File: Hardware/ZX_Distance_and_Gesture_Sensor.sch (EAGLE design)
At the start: 48 parts, among them Q1 MMBT2222A, Q2 MOSFET-NCHANNEL2N7002PW, U1 BRM-2508VERT

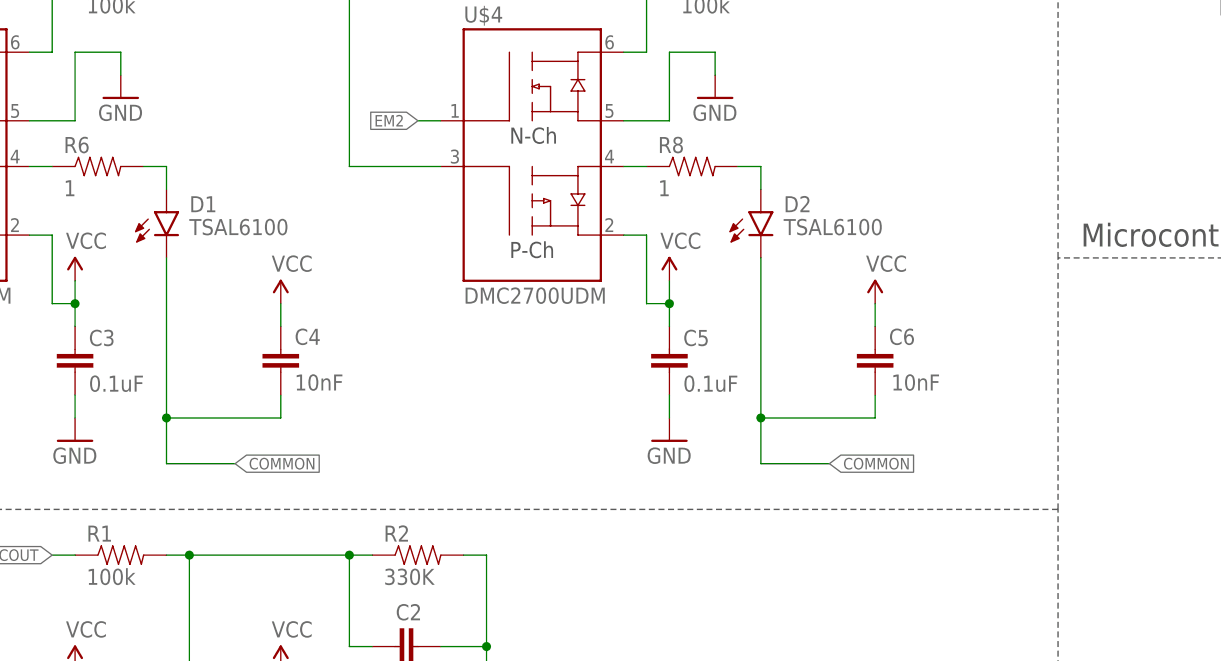
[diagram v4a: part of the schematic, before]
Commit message: Added second option for SMT IR LEDs. Added solder pads for blinders.
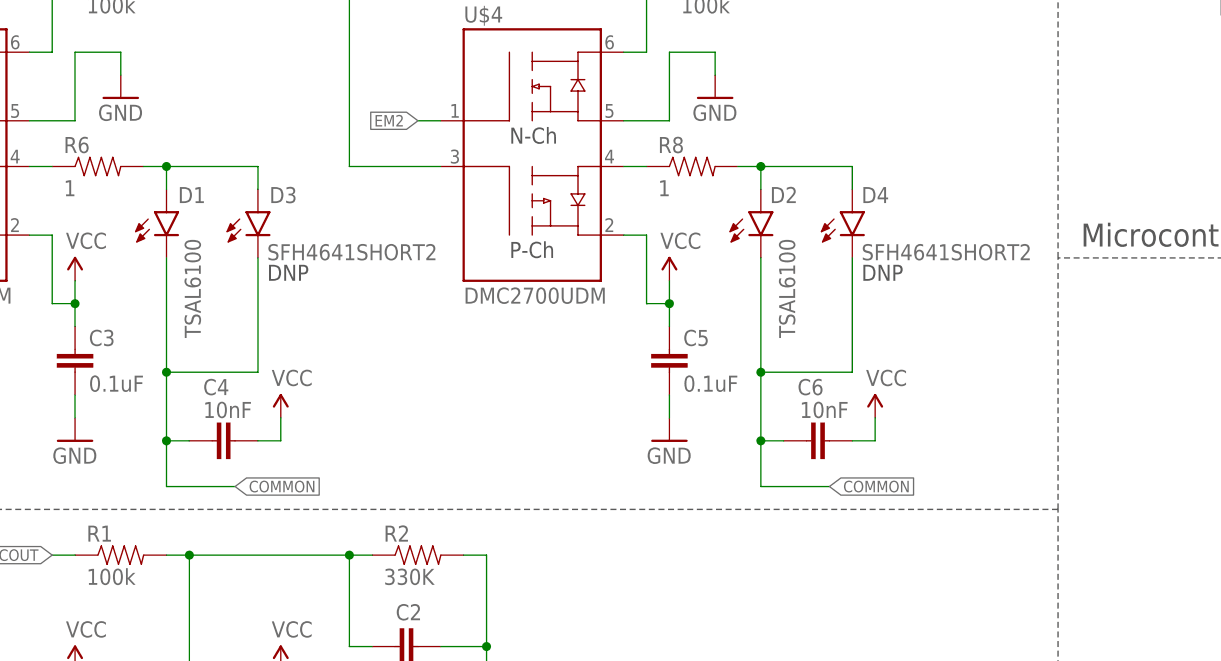
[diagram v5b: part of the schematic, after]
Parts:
- added D3, D4: SFH4641SHORT2, SparkFun-LED:SFH4641SHORT2
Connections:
- net COMMON: now also D3.C, D4.C
- net N$12: now also D4.A
- net N$7: now also D3.A
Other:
- note added: "DNP"
- moved on the sheet: C4, C6
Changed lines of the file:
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@@
 <setting verticaltext="up"/>
 </settings>
-<grid distance="0.1" unitdist="inch" unit="inch" style="lines" multiple="1" display="no" altdistance="0.01" altunitdist="inch" altunit="inch"/>
+<grid distance="0.1" unitdist="inch" unit="inch" style="lines" multiple="1" display="yes" altdistance="0.01" altunitdist="inch" altunit="inch"/>
 <layers>
 <layer number="1" name="Top" color="4" fill="1" visible="no" active="no"/>
@@
 <layer number="111" name="LPC17xx" color="7" fill="1" visible="yes" active="yes"/>
 <layer number="112" name="tSilk" color="7" fill="1" visible="yes" active="yes"/>
+<layer number="113" name="IDFDebug" color="7" fill="1" visible="yes" active="yes"/>
 <layer number="116" name="Patch_BOT" color="9" fill="4" visible="yes" active="yes"/>
 <layer number="121" name="_tsilk" color="7" fill="1" visible="yes" active="yes"/>
@@
 <part name="GND16" library="SparkFun-Aesthetics" deviceset="GND" device=""/>
 <part name="U$6" library="SparkFun-Aesthetics" deviceset="GESTURESENSE_LOGOS" device="TEXT"/>
+<part name="D3" library="SparkFun-LED" deviceset="SFH4641" device="SHORT2"/>
+<part name="D4" library="SparkFun-LED" deviceset="SFH4641" device="SHORT2"/>
 </parts>
 <sheets>
@@
 <text x="50.8" y="149.86" size="1.778" layer="97" align="center-right">DR</text>
 <text x="7.62" y="149.86" size="1.778" layer="97" align="center-right">NC</text>
+<text x="59.436" y="96.52" size="1.778" layer="97">DNP</text>
+<text x="125.476" y="96.52" size="1.778" layer="97">DNP</text>
 </plain>
 <instances>
@@
 <instance part="GND6" gate="1" x="91.44" y="5.08"/>
 <instance part="D1" gate="G$1" x="48.26" y="104.14" smashed="yes">
-<attribute name="NAME" x="50.8" y="104.14" size="1.778" layer="95"/>
-<attribute name="VARIANT" x="50.8" y="101.6" size="1.778" layer="96"/>
+<attribute name="NAME" x="49.53" y="105.156" size="1.778" layer="95"/>
+<attribute name="VARIANT" x="52.07" y="90.17" size="1.778" layer="96" rot="R90"/>
 </instance>
 <instance part="R5" gate="G$1" x="43.18" y="129.54"/>
@@
 <attribute name="VALUE" x="39.624" y="84.201" size="1.778" layer="96"/>
 </instance>
-<instance part="C4" gate="G$1" x="60.96" y="88.9" smashed="yes" rot="R180">
-<attribute name="NAME" x="62.484" y="89.408" size="1.778" layer="95"/>
-<attribute name="VALUE" x="62.484" y="84.328" size="1.778" layer="96"/>
+<instance part="C4" gate="G$1" x="55.88" y="78.74" smashed="yes" rot="R90">
+<attribute name="NAME" x="52.324" y="83.82" size="1.778" layer="95"/>
+<attribute name="VALUE" x="52.324" y="81.28" size="1.778" layer="96"/>
 </instance>
 <instance part="SUPPLY5" gate="G$1" x="38.1" y="96.52"/>
-<instance part="SUPPLY6" gate="G$1" x="60.96" y="93.98"/>
+<instance part="SUPPLY6" gate="G$1" x="60.96" y="81.28"/>
 <instance part="GND7" gate="1" x="38.1" y="78.74"/>
 <instance part="GND8" gate="1" x="43.18" y="116.84"/>
@@
 <attribute name="VALUE" x="105.664" y="84.201" size="1.778" layer="96"/>
 </instance>
-<instance part="C6" gate="G$1" x="127" y="88.9" smashed="yes" rot="R180">
-<attribute name="NAME" x="128.524" y="89.408" size="1.778" layer="95"/>
-<attribute name="VALUE" x="128.778" y="84.328" size="1.778" layer="96"/>
-</instance>
-<instance part="SUPPLY9" gate="G$1" x="127" y="93.98"/>
+<instance part="C6" gate="G$1" x="121.92" y="78.74" smashed="yes" rot="R90">
+<attribute name="NAME" x="118.364" y="83.82" size="1.778" layer="95"/>
+<attribute name="VALUE" x="118.618" y="81.28" size="1.778" layer="96"/>
+</instance>
+<instance part="SUPPLY9" gate="G$1" x="127" y="81.28"/>
 <instance part="SUPPLY10" gate="G$1" x="104.14" y="96.52"/>
 <instance part="GND10" gate="1" x="104.14" y="78.74"/>
@@
 <instance part="SUPPLY11" gate="G$1" x="170.18" y="68.58"/>
 <instance part="D2" gate="G$1" x="114.3" y="104.14" smashed="yes">
-<attribute name="NAME" x="116.84" y="104.14" size="1.778" layer="95"/>
-<attribute name="VARIANT" x="116.84" y="101.6" size="1.778" layer="96"/>
+<attribute name="NAME" x="115.316" y="105.156" size="1.778" layer="95"/>
+<attribute name="VARIANT" x="118.11" y="90.17" size="1.778" layer="96" rot="R90"/>
 </instance>
 <instance part="SUPPLY12" gate="G$1" x="223.52" y="91.44"/>
@@
 <instance part="GND16" gate="1" x="172.72" y="78.74"/>
 <instance part="U$6" gate="G$1" x="127" y="22.86"/>
+<instance part="D3" gate="G$1" x="58.42" y="104.14" smashed="yes">
+<attribute name="NAME" x="59.69" y="105.156" size="1.778" layer="95"/>
+<attribute name="VALUE" x="59.436" y="98.806" size="1.778" layer="96"/>
+</instance>
+<instance part="D4" gate="G$1" x="124.46" y="104.14" smashed="yes">
+<attribute name="NAME" x="125.476" y="105.156" size="1.778" layer="95"/>
+<attribute name="VALUE" x="125.476" y="98.806" size="1.778" layer="96"/>
+</instance>
 </instances>
 <busses>
@@
 <pinref part="U$2" gate="G$1" pin="V+"/>
 <wire x1="60.96" y1="53.34" x2="60.96" y2="50.8" width="0.1524" layer="91"/>
-</segment>
-<segment>
-<pinref part="SUPPLY6" gate="G$1" pin="VCC"/>
-<pinref part="C4" gate="G$1" pin="2"/>
-<wire x1="60.96" y1="93.98" x2="60.96" y2="91.44" width="0.1524" layer="91"/>
 </segment>
 <segment>
@@
 </segment>
 <segment>
-<pinref part="C6" gate="G$1" pin="2"/>
-<pinref part="SUPPLY9" gate="G$1" pin="VCC"/>
-<wire x1="127" y1="91.44" x2="127" y2="93.98" width="0.1524" layer="91"/>
-</segment>
-<segment>
 <pinref part="SUPPLY10" gate="G$1" pin="VCC"/>
 <pinref part="C5" gate="G$1" pin="1"/>
@@
 <wire x1="172.72" y1="86.36" x2="172.72" y2="88.9" width="0.1524" layer="91"/>
 <pinref part="SUPPLY16" gate="G$1" pin="VCC"/>
+</segment>
+<segment>
+<pinref part="C4" gate="G$1" pin="2"/>
+<pinref part="SUPPLY6" gate="G$1" pin="VCC"/>
+<wire x1="58.42" y1="78.74" x2="60.96" y2="78.74" width="0.1524" layer="91"/>
+<wire x1="60.96" y1="78.74" x2="60.96" y2="81.28" width="0.1524" layer="91"/>
+</segment>
+<segment>
+<pinref part="C6" gate="G$1" pin="2"/>
+<pinref part="SUPPLY9" gate="G$1" pin="VCC"/>
+<wire x1="124.46" y1="78.74" x2="127" y2="78.74" width="0.1524" layer="91"/>
+<wire x1="127" y1="78.74" x2="127" y2="81.28" width="0.1524" layer="91"/>
 </segment>
 </net>
@@
 <segment>
 <pinref part="D1" gate="G$1" pin="C"/>
-<wire x1="48.26" y1="99.06" x2="48.26" y2="81.28" width="0.1524" layer="91"/>
-<wire x1="48.26" y1="81.28" x2="48.26" y2="76.2" width="0.1524" layer="91"/>
-<wire x1="48.26" y1="76.2" x2="55.88" y2="76.2" width="0.1524" layer="91"/>
-<label x="55.88" y="76.2" size="1.27" layer="95" xref="yes"/>
+<wire x1="48.26" y1="99.06" x2="48.26" y2="86.36" width="0.1524" layer="91"/>
+<wire x1="48.26" y1="86.36" x2="48.26" y2="78.74" width="0.1524" layer="91"/>
+<wire x1="48.26" y1="78.74" x2="48.26" y2="73.66" width="0.1524" layer="91"/>
+<wire x1="48.26" y1="73.66" x2="55.88" y2="73.66" width="0.1524" layer="91"/>
+<label x="55.88" y="73.66" size="1.27" layer="95" xref="yes"/>
 <pinref part="C4" gate="G$1" pin="1"/>
-<wire x1="60.96" y1="83.82" x2="60.96" y2="81.28" width="0.1524" layer="91"/>
-<wire x1="60.96" y1="81.28" x2="48.26" y2="81.28" width="0.1524" layer="91"/>
-<junction x="48.26" y="81.28"/>
-</segment>
-<segment>
-<wire x1="114.3" y1="99.06" x2="114.3" y2="81.28" width="0.1524" layer="91"/>
-<wire x1="114.3" y1="81.28" x2="114.3" y2="76.2" width="0.1524" layer="91"/>
-<wire x1="114.3" y1="76.2" x2="121.92" y2="76.2" width="0.1524" layer="91"/>
+<wire x1="48.26" y1="78.74" x2="50.8" y2="78.74" width="0.1524" layer="91"/>
+<junction x="48.26" y="78.74"/>
+<pinref part="D3" gate="G$1" pin="C"/>
+<wire x1="58.42" y1="99.06" x2="58.42" y2="86.36" width="0.1524" layer="91"/>
+<wire x1="58.42" y1="86.36" x2="48.26" y2="86.36" width="0.1524" layer="91"/>
+<junction x="48.26" y="86.36"/>
+</segment>
+<segment>
+<wire x1="114.3" y1="99.06" x2="114.3" y2="86.36" width="0.1524" layer="91"/>
+<wire x1="114.3" y1="86.36" x2="114.3" y2="78.74" width="0.1524" layer="91"/>
+<wire x1="114.3" y1="78.74" x2="114.3" y2="73.66" width="0.1524" layer="91"/>
+<wire x1="114.3" y1="73.66" x2="121.92" y2="73.66" width="0.1524" layer="91"/>
+<label x="121.92" y="73.66" size="1.27" layer="95" xref="yes"/>
+<pinref part="D2" gate="G$1" pin="C"/>
 <pinref part="C6" gate="G$1" pin="1"/>
-<wire x1="127" y1="83.82" x2="127" y2="81.28" width="0.1524" layer="91"/>
-<wire x1="127" y1="81.28" x2="114.3" y2="81.28" width="0.1524" layer="91"/>
-<junction x="114.3" y="81.28"/>
-<label x="121.92" y="76.2" size="1.27" layer="95" xref="yes"/>
-<pinref part="D2" gate="G$1" pin="C"/>
+<wire x1="116.84" y1="78.74" x2="114.3" y2="78.74" width="0.1524" layer="91"/>
+<junction x="114.3" y="78.74"/>
+<pinref part="D4" gate="G$1" pin="C"/>
+<wire x1="124.46" y1="99.06" x2="124.46" y2="86.36" width="0.1524" layer="91"/>
+<wire x1="124.46" y1="86.36" x2="114.3" y2="86.36" width="0.1524" layer="91"/>
+<junction x="114.3" y="86.36"/>
 </segment>
 </net>
@@
 <wire x1="45.72" y1="109.22" x2="48.26" y2="109.22" width="0.1524" layer="91"/>
 <wire x1="48.26" y1="109.22" x2="48.26" y2="106.68" width="0.1524" layer="91"/>
+<pinref part="D3" gate="G$1" pin="A"/>
+<wire x1="48.26" y1="109.22" x2="58.42" y2="109.22" width="0.1524" layer="91"/>
+<wire x1="58.42" y1="109.22" x2="58.42" y2="106.68" width="0.1524" layer="91"/>
+<junction x="48.26" y="109.22"/>
 </segment>
 </net>
@@
 <wire x1="114.3" y1="109.22" x2="114.3" y2="106.68" width="0.1524" layer="91"/>
 <pinref part="D2" gate="G$1" pin="A"/>
-</segment>
-</net>
+<pinref part="D4" gate="G$1" pin="A"/>
+<wire x1="114.3" y1="109.22" x2="124.46" y2="109.22" width="0.1524" layer="91"/>
+<wire x1="124.46" y1="109.22" x2="124.46" y2="106.68" width="0.1524" layer="91"/>
+<junction x="114.3" y="109.22"/>
+</segment>
+</net>
